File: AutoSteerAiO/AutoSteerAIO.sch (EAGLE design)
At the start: 88 parts, among them K4 CB1A-P-12V, U1 VX7805-1000

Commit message: Add files via upload
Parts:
- added 5V2: CONNECTOR 1x2 PINS, SparkFun-Connectors:CONN_02
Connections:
- net +5V: now also 5V2.2
- net GND: now also 5V2.1
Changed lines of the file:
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@@
 <part name="P+17" library="supply1" library_urn="urn:adsk.eagle:library:371" deviceset="+15V" device=""/>
 <part name="GND32" library="supply1" library_urn="urn:adsk.eagle:library:371" deviceset="GND" device=""/>
+<part name="5V2" library="SparkFun-Connectors" library_urn="urn:adsk.eagle:library:513" deviceset="CONN_02" device="" package3d_urn="urn:adsk.eagle:package:38039/1" value="CONNECTOR 1x2 PINS">
+<attribute name="MF" value=""/>
+<attribute name="MPN" value=""/>
+<attribute name="OC_NEWARK" value="unknown"/>
+</part>
+<part name="P+18" library="supply1" library_urn="urn:adsk.eagle:library:371" deviceset="+5V" device=""/>
+<part name="GND35" library="supply1" library_urn="urn:adsk.eagle:library:371" deviceset="GND" device=""/>
 </parts>
 <sheets>
@@
 <attribute name="VALUE" x="133.35" y="217.17" size="1.778" layer="96"/>
 </instance>
+<instance part="5V2" gate="G$1" x="7.62" y="222.25" smashed="yes">
+<attribute name="NAME" x="5.08" y="227.838" size="1.778" layer="95" font="vector"/>
+<attribute name="OC_NEWARK" x="7.62" y="222.25" size="1.778" layer="96" display="off"/>
+<attribute name="MF" x="7.62" y="222.25" size="1.778" layer="96" display="off"/>
+<attribute name="MPN" x="7.62" y="222.25" size="1.778" layer="96" display="off"/>
+</instance>
+<instance part="P+18" gate="1" x="21.59" y="224.79" smashed="yes" rot="R270">
+<attribute name="VALUE" x="16.51" y="227.33" size="1.778" layer="96"/>
+</instance>
+<instance part="GND35" gate="1" x="19.05" y="217.17" smashed="yes">
+<attribute name="VALUE" x="16.51" y="214.63" size="1.778" layer="96"/>
+</instance>
 </instances>
 <busses>
@@
 <pinref part="P+15" gate="1" pin="+5V"/>
 <wire x1="15.24" y1="212.09" x2="19.05" y2="212.09" width="0.1524" layer="91"/>
+</segment>
+<segment>
+<pinref part="5V2" gate="G$1" pin="2"/>
+<pinref part="P+18" gate="1" pin="+5V"/>
+<wire x1="15.24" y1="224.79" x2="19.05" y2="224.79" width="0.1524" layer="91"/>
 </segment>
 </net>
@@
 <wire x1="132.08" y1="222.25" x2="135.89" y2="222.25" width="0.1524" layer="91"/>
 </segment>
+<segment>
+<pinref part="GND35" gate="1" pin="GND"/>
+<pinref part="5V2" gate="G$1" pin="1"/>
+<wire x1="19.05" y1="219.71" x2="19.05" y2="222.25" width="0.1524" layer="91"/>
+<wire x1="19.05" y1="222.25" x2="15.24" y2="222.25" width="0.1524" layer="91"/>
+</segment>
 </net>

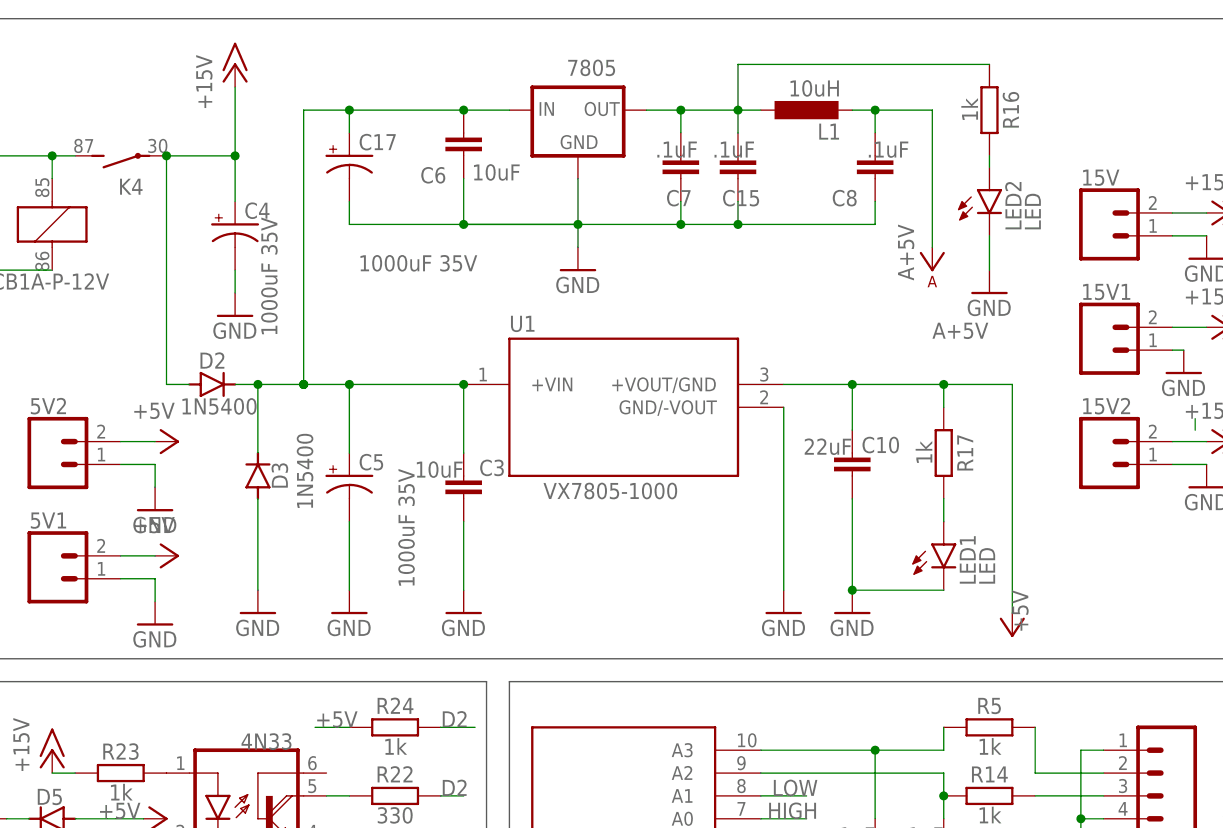
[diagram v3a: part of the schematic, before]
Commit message: Add files via upload
I removed the capacitors and the inductor has no need for them
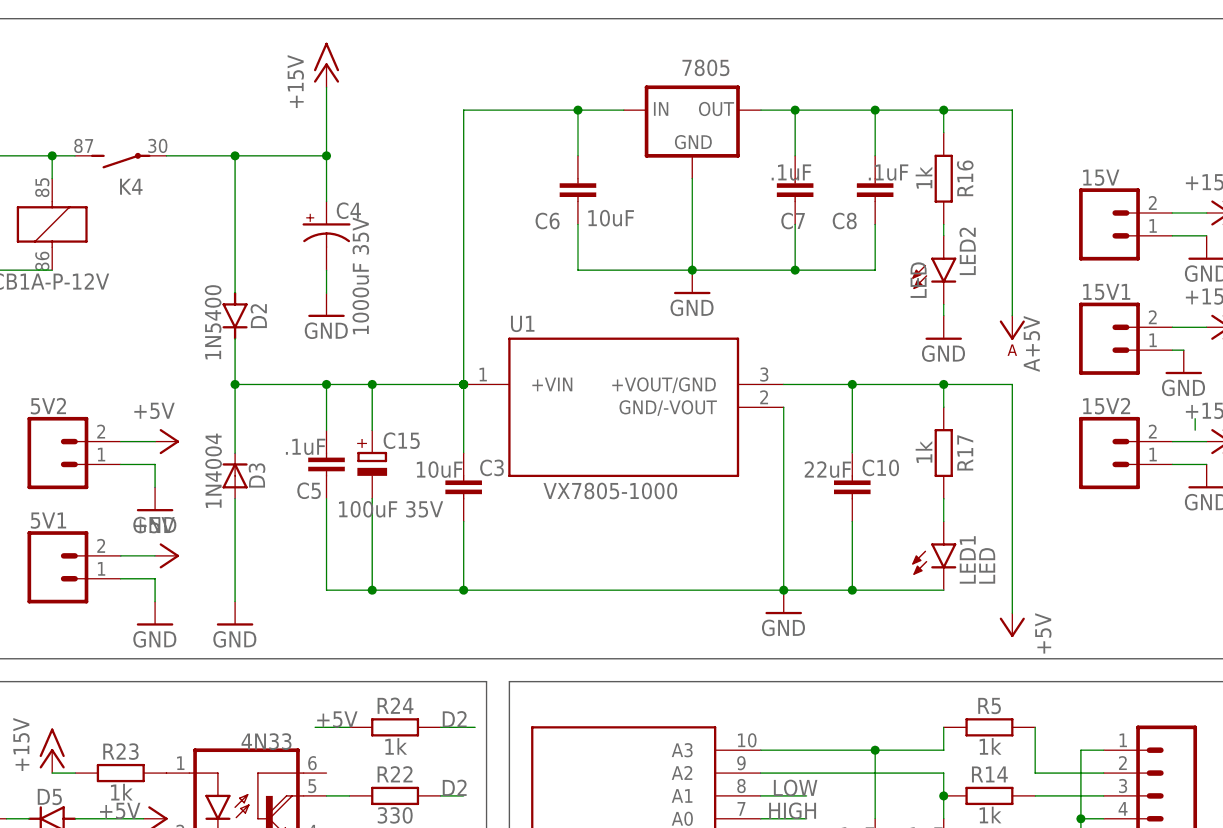
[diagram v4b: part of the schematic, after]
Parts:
- removed C17: 1000uF 35V, SparkFun-Capacitors:1000UF-RADIAL-5MM-25V-20%
- removed L1: 10uH, rcl:L-EU0207/10
- C15: value .1uF -> 100uF 35V; device resistor:C-EU050-024X044 -> rcl:CPOL-EUE2.5-6; OC_NEWARK unknown -> (none)
- C5: value 1000uF 35V -> .1uF; device SparkFun-Capacitors:1000UF-RADIAL-5MM-25V-20% -> resistor:C-EU050-024X044
- D3: value 1N5400 -> 1N4004; device #Diode 2:1N5400 -> #adafruit:1N4004
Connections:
- removed net N$25: 7805.OUT, C15.2, C7.2, L1.1, R16.1
- net A+5V: now also 7805.OUT, C7.2, R16.1; no longer L1.2
- net GND: now also C15.-, C5.1; no longer C15.1, C17.-, C5.-
- net N$26: now also C15.+, C5.2; no longer C17.+, C5.+
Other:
- moved on the sheet: 7805, C10, C4, C6, C7, C8, D2, LED2, R16

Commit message: Add files via upload
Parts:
- removed R4: 330, resistor:R-EU_0207/7
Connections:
- net GND: no longer R4.2
- net LOW.: no longer R4.1
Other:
- moved on the sheet: D4, WAS_D
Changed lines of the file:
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@@
 <?xml version="1.0" encoding="utf-8"?>
 <!DOCTYPE eagle SYSTEM "eagle.dtd">
-<eagle version="9.5.2">
+<eagle version="9.6.1">
 <drawing>
 <settings>
@@
 <attribute name="OC_NEWARK" value="unknown"/>
 </part>
-<part name="R4" library="resistor" library_urn="urn:adsk.eagle:library:348" deviceset="R-EU_" device="0207/7" package3d_urn="urn:adsk.eagle:package:23493/2" value="330">
-<attribute name="MF" value=""/>
-<attribute name="MPN" value=""/>
-<attribute name="OC_NEWARK" value="unknown"/>
-</part>
 <part name="TO_SECTION" library="SparkFun-Connectors" library_urn="urn:adsk.eagle:library:513" deviceset="CONN_02" device="" package3d_urn="urn:adsk.eagle:package:38039/1" value="CONNECTOR 1x2 PINS">
 <attribute name="MF" value=""/>
@@
 <part name="GND26" library="supply1" library_urn="urn:adsk.eagle:library:371" deviceset="GND" device=""/>
 <part name="P+14" library="supply1" library_urn="urn:adsk.eagle:library:371" deviceset="+5V" device=""/>
-<part name="GND27" library="supply1" library_urn="urn:adsk.eagle:library:371" deviceset="GND" device=""/>
 <part name="GND29" library="supply1" library_urn="urn:adsk.eagle:library:371" deviceset="GND" device=""/>
 <part name="GND28" library="supply1" library_urn="urn:adsk.eagle:library:371" deviceset="GND" device=""/>
@@
 <attribute name="MPN" x="71.12" y="177.8" size="1.778" layer="96" display="off"/>
 </instance>
-<instance part="WAS_D" gate="G$1" x="66.04" y="142.24" smashed="yes">
-<attribute name="NAME" x="60.96" y="150.368" size="1.778" layer="95" font="vector"/>
-<attribute name="OC_NEWARK" x="66.04" y="142.24" size="1.778" layer="96" display="off"/>
-<attribute name="MF" x="66.04" y="142.24" size="1.778" layer="96" display="off"/>
-<attribute name="MPN" x="66.04" y="142.24" size="1.778" layer="96" display="off"/>
+<instance part="WAS_D" gate="G$1" x="73.66" y="142.24" smashed="yes">
+<attribute name="NAME" x="68.58" y="150.368" size="1.778" layer="95" font="vector"/>
+<attribute name="OC_NEWARK" x="73.66" y="142.24" size="1.778" layer="96" display="off"/>
+<attribute name="MF" x="73.66" y="142.24" size="1.778" layer="96" display="off"/>
+<attribute name="MPN" x="73.66" y="142.24" size="1.778" layer="96" display="off"/>
 </instance>
 <instance part="STEER-SWITCH" gate="J$1" x="-5.08" y="157.48" smashed="yes">
@@
 <attribute name="MPN" x="129.54" y="147.32" size="1.778" layer="96" display="off"/>
 </instance>
-<instance part="D4" gate="1" x="90.17" y="139.7" smashed="yes" rot="R180">
-<attribute name="NAME" x="91.44" y="143.0274" size="1.778" layer="95" rot="R180"/>
-<attribute name="VALUE" x="93.98" y="138.2014" size="1.778" layer="96" rot="R180"/>
-<attribute name="OC_NEWARK" x="90.17" y="139.7" size="1.778" layer="96" display="off"/>
-<attribute name="MF" x="90.17" y="139.7" size="1.778" layer="96" display="off"/>
-<attribute name="MPN" x="90.17" y="139.7" size="1.778" layer="96" display="off"/>
+<instance part="D4" gate="1" x="95.25" y="139.7" smashed="yes" rot="R180">
+<attribute name="NAME" x="96.52" y="143.0274" size="1.778" layer="95" rot="R180"/>
+<attribute name="VALUE" x="99.06" y="138.2014" size="1.778" layer="96" rot="R180"/>
+<attribute name="OC_NEWARK" x="95.25" y="139.7" size="1.778" layer="96" display="off"/>
+<attribute name="MF" x="95.25" y="139.7" size="1.778" layer="96" display="off"/>
+<attribute name="MPN" x="95.25" y="139.7" size="1.778" layer="96" display="off"/>
 </instance>
 <instance part="P+10" gate="1" x="7.62" y="167.64" smashed="yes">
@@
 <attribute name="MPN" x="27.94" y="220.98" size="1.778" layer="96" display="off"/>
 </instance>
-<instance part="R4" gate="G$1" x="96.52" y="153.035" smashed="yes">
-<attribute name="NAME" x="96.52" y="154.5336" size="1.778" layer="95" rot="R180" align="top-center"/>
-<attribute name="VALUE" x="96.52" y="151.765" size="1.778" layer="95" rot="R180" align="bottom-center"/>
-<attribute name="OC_NEWARK" x="96.52" y="153.035" size="1.778" layer="96" display="off"/>
-<attribute name="MF" x="96.52" y="153.035" size="1.778" layer="96" display="off"/>
-<attribute name="MPN" x="96.52" y="153.035" size="1.778" layer="96" display="off"/>
-</instance>
 <instance part="TO_SECTION" gate="G$1" x="129.54" y="165.1" smashed="yes">
 <attribute name="NAME" x="129.54" y="171.958" size="1.778" layer="95" font="vector" align="center"/>
@@
 </instance>
 <instance part="P+14" gate="1" x="190.5" y="179.07" smashed="yes" rot="R180"/>
-<instance part="GND27" gate="1" x="101.6" y="147.955" smashed="yes">
-<attribute name="VALUE" x="99.06" y="145.415" size="1.778" layer="96"/>
-</instance>
 <instance part="GND29" gate="1" x="121.92" y="139.7" smashed="yes">
 <attribute name="VALUE" x="119.38" y="137.16" size="1.778" layer="96"/>
@@
 <attribute name="VALUE" x="115.57" y="238.76" size="1.778" layer="96" rot="R270"/>
 </instance>
-<instance part="U$15" gate="G$1" x="101.6" y="137.16" smashed="yes" rot="R180">
-<attribute name="VALUE" x="102.87" y="137.16" size="1.778" layer="96"/>
+<instance part="U$15" gate="G$1" x="109.22" y="137.16" smashed="yes" rot="R180">
+<attribute name="VALUE" x="110.49" y="137.16" size="1.778" layer="96"/>
 </instance>
 <instance part="U$16" gate="G$1" x="91.44" y="162.56" smashed="yes" rot="R180">
@@
 <segment>
 <pinref part="WAS_D" gate="G$1" pin="3"/>
-<label x="73.66" y="144.78" size="1.778" layer="95"/>
+<label x="81.28" y="144.78" size="1.778" layer="95"/>
 <pinref part="R11" gate="G$1" pin="1"/>
-<wire x1="71.12" y1="144.78" x2="104.14" y2="144.78" width="0.1524" layer="91"/>
+<wire x1="78.74" y1="144.78" x2="104.14" y2="144.78" width="0.1524" layer="91"/>
 </segment>
 </net>
@@
 <segment>
 <pinref part="WAS_D" gate="G$1" pin="4"/>
-<label x="73.66" y="147.32" size="1.778" layer="95"/>
+<label x="81.28" y="147.32" size="1.778" layer="95"/>
 <pinref part="R10" gate="G$1" pin="1"/>
-<wire x1="71.12" y1="147.32" x2="86.36" y2="147.32" width="0.1524" layer="91"/>
-<wire x1="104.14" y1="157.48" x2="91.44" y2="157.48" width="0.1524" layer="91"/>
-<wire x1="91.44" y1="157.48" x2="86.36" y2="157.48" width="0.1524" layer="91"/>
-<wire x1="86.36" y1="157.48" x2="86.36" y2="147.32" width="0.1524" layer="91"/>
-<pinref part="R4" gate="G$1" pin="1"/>
-<wire x1="91.44" y1="153.035" x2="91.44" y2="157.48" width="0.1524" layer="91"/>
-<junction x="91.44" y="157.48"/>
+<wire x1="78.74" y1="147.32" x2="99.06" y2="147.32" width="0.1524" layer="91"/>
+<wire x1="104.14" y1="157.48" x2="99.06" y2="157.48" width="0.1524" layer="91"/>
+<wire x1="99.06" y1="157.48" x2="99.06" y2="147.32" width="0.1524" layer="91"/>
 </segment>
 </net>
@@
 <segment>
 <pinref part="WAS_D" gate="G$1" pin="2"/>
-<label x="73.66" y="142.24" size="1.778" layer="95"/>
+<label x="81.28" y="142.24" size="1.778" layer="95"/>
 <pinref part="C13" gate="G$1" pin="1"/>
 <pinref part="C14" gate="G$1" pin="1"/>
@@
 <junction x="129.54" y="142.24"/>
 <wire x1="129.54" y1="142.24" x2="137.16" y2="142.24" width="0.1524" layer="91"/>
-<wire x1="71.12" y1="142.24" x2="121.92" y2="142.24" width="0.1524" layer="91"/>
+<wire x1="78.74" y1="142.24" x2="121.92" y2="142.24" width="0.1524" layer="91"/>
 <pinref part="GND29" gate="1" pin="GND"/>
 <junction x="121.92" y="142.24"/>
@@
 </segment>
 <segment>
-<pinref part="R4" gate="G$1" pin="2"/>
-<pinref part="GND27" gate="1" pin="GND"/>
-<wire x1="101.6" y1="153.035" x2="101.6" y2="150.495" width="0.1524" layer="91"/>
-</segment>
-<segment>
 <pinref part="STEER-SWITCH" gate="J$1" pin="1"/>
 <pinref part="GND16" gate="1" pin="GND"/>
@@
 <segment>
 <pinref part="WAS_D" gate="G$1" pin="1"/>
-<wire x1="71.12" y1="139.7" x2="87.63" y2="139.7" width="0.1524" layer="91"/>
+<wire x1="78.74" y1="139.7" x2="92.71" y2="139.7" width="0.1524" layer="91"/>
 <pinref part="D4" gate="1" pin="C"/>
-<label x="73.66" y="139.7" size="1.778" layer="95"/>
+<label x="81.28" y="139.7" size="1.778" layer="95"/>
 </segment>
 </net>
@@
 <segment>
 <pinref part="D4" gate="1" pin="A"/>
-<wire x1="92.71" y1="139.7" x2="101.6" y2="139.7" width="0.1524" layer="91"/>
+<wire x1="97.79" y1="139.7" x2="109.22" y2="139.7" width="0.1524" layer="91"/>
 <pinref part="U$15" gate="G$1" pin="A+5V"/>
 </segment>

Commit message: Add files via upload
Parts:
- removed OR: CONNECTOR 1x3 PINS, SparkFun-Connectors:CONN_03
- added 5V3: CONNECTOR 1x2 PINS, SparkFun-Connectors:CONN_02
- added J1: (no value), SparkFun-Connectors:CONN_01
- added U$1: MD13S, #Motor Drivers:MD13S
- added U$2: IBT2, #Motor Drivers:IBT2
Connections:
- removed net EN: IBT2.3, IBT2.4, OR.2
- removed net SAO: MMA8542.SAO
- new net A6: 0.2, PCB1.A6
- new net A7: 0.1, PCB1.A7
- net +5V: now also 5V3.2
- net A0: now also 1.3; no longer 1.2
- net A1: now also 1.2; no longer 1.1
- net A2: now also 1.1; no longer 0.2
- net A3: now also 0.3; no longer 0.1
- net D5: now also J1.1; no longer OR.1
- net DIR: now also IBT2.3, IBT2.4; no longer OR.3
- net GND: now also 5V3.1, MMA8542.SAO; no longer 0.3, 1.3
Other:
- moved on the sheet: 0

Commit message: Add files via upload
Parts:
- added RST: CONNECTOR 1x2 PINS, SparkFun-Connectors:CONN_02
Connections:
- new net RST: PCB1.RST., RST.2
- net GND: now also RST.1
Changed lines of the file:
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@@
 <part name="J1" library="SparkFun-Connectors" library_urn="urn:adsk.eagle:library:513" deviceset="CONN_01" device="" package3d_urn="urn:adsk.eagle:package:38028/1"/>
 <part name="GND24" library="supply1" library_urn="urn:adsk.eagle:library:371" deviceset="GND" device=""/>
+<part name="RST" library="SparkFun-Connectors" library_urn="urn:adsk.eagle:library:513" deviceset="CONN_02" device="" package3d_urn="urn:adsk.eagle:package:38039/1" value="CONNECTOR 1x2 PINS">
+<attribute name="MF" value=""/>
+<attribute name="MPN" value=""/>
+<attribute name="OC_NEWARK" value="unknown"/>
+</part>
 </parts>
 <sheets>
@@
 <attribute name="VALUE" x="58.42" y="114.3" size="1.778" layer="96"/>
 </instance>
+<instance part="RST" gate="G$1" x="195.58" y="167.64" smashed="yes">
+<attribute name="NAME" x="195.58" y="174.498" size="1.778" layer="95" font="vector" align="center"/>
+<attribute name="OC_NEWARK" x="195.58" y="167.64" size="1.778" layer="96" display="off"/>
+<attribute name="MF" x="195.58" y="167.64" size="1.778" layer="96" display="off"/>
+<attribute name="MPN" x="195.58" y="167.64" size="1.778" layer="96" display="off"/>
+</instance>
 </instances>
 <busses>
@@
 <wire x1="215.9" y1="139.7" x2="215.9" y2="147.32" width="0.1524" layer="91"/>
 <pinref part="PCB1" gate="G$1" pin="GND"/>
-<wire x1="177.8" y1="134.62" x2="172.72" y2="134.62" width="0.1524" layer="91"/>
-<wire x1="172.72" y1="134.62" x2="163.83" y2="134.62" width="0.1524" layer="91"/>
+<wire x1="177.8" y1="134.62" x2="167.64" y2="134.62" width="0.1524" layer="91"/>
+<wire x1="167.64" y1="134.62" x2="163.83" y2="134.62" width="0.1524" layer="91"/>
 <pinref part="GND33" gate="1" pin="GND"/>
-<wire x1="215.9" y1="147.32" x2="172.72" y2="147.32" width="0.1524" layer="91"/>
-<wire x1="172.72" y1="134.62" x2="172.72" y2="147.32" width="0.1524" layer="91"/>
-<junction x="172.72" y="134.62"/>
+<wire x1="215.9" y1="147.32" x2="167.64" y2="147.32" width="0.1524" layer="91"/>
+<wire x1="167.64" y1="134.62" x2="167.64" y2="147.32" width="0.1524" layer="91"/>
+<junction x="167.64" y="134.62"/>
 </segment>
 <segment>
@@
 <wire x1="68.58" y1="119.38" x2="60.96" y2="119.38" width="0.1524" layer="91"/>
 <pinref part="GND24" gate="1" pin="GND"/>
+</segment>
+<segment>
+<pinref part="RST" gate="G$1" pin="1"/>
+<wire x1="203.2" y1="167.64" x2="210.82" y2="167.64" width="0.1524" layer="91"/>
+<label x="205.74" y="167.64" size="1.778" layer="95"/>
 </segment>
 </net>
@@
 </segment>
 </net>
+<net name="RST" class="0">
+<segment>
+<pinref part="PCB1" gate="G$1" pin="RST."/>
+<wire x1="210.82" y1="137.16" x2="220.98" y2="137.16" width="0.1524" layer="91"/>
+<label x="215.9" y="137.16" size="1.778" layer="95"/>
+</segment>
+<segment>
+<pinref part="RST" gate="G$1" pin="2"/>
+<wire x1="203.2" y1="170.18" x2="210.82" y2="170.18" width="0.1524" layer="91"/>
+<label x="205.74" y="170.18" size="1.778" layer="95"/>
+</segment>
+</net>
